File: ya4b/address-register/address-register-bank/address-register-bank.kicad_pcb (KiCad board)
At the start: 4 copper layers, 114.3 x 90.3 mm, 99 parts, among them J1 Conn_01x38_Male, U1 GAL16V8, U10 74LS169, U11 74LS169, U12 74LS541, U13 74LS169, U14 74LS169, U15 74LS541, U16 74LS169, U17 74LS169, U18 74LS541, U2 GAL22V10, U3 74HCT04, U4 74HCT00, U5 74LS157, U6 74LS157, U7 74LS169, U8 74LS169, U9 74LS541

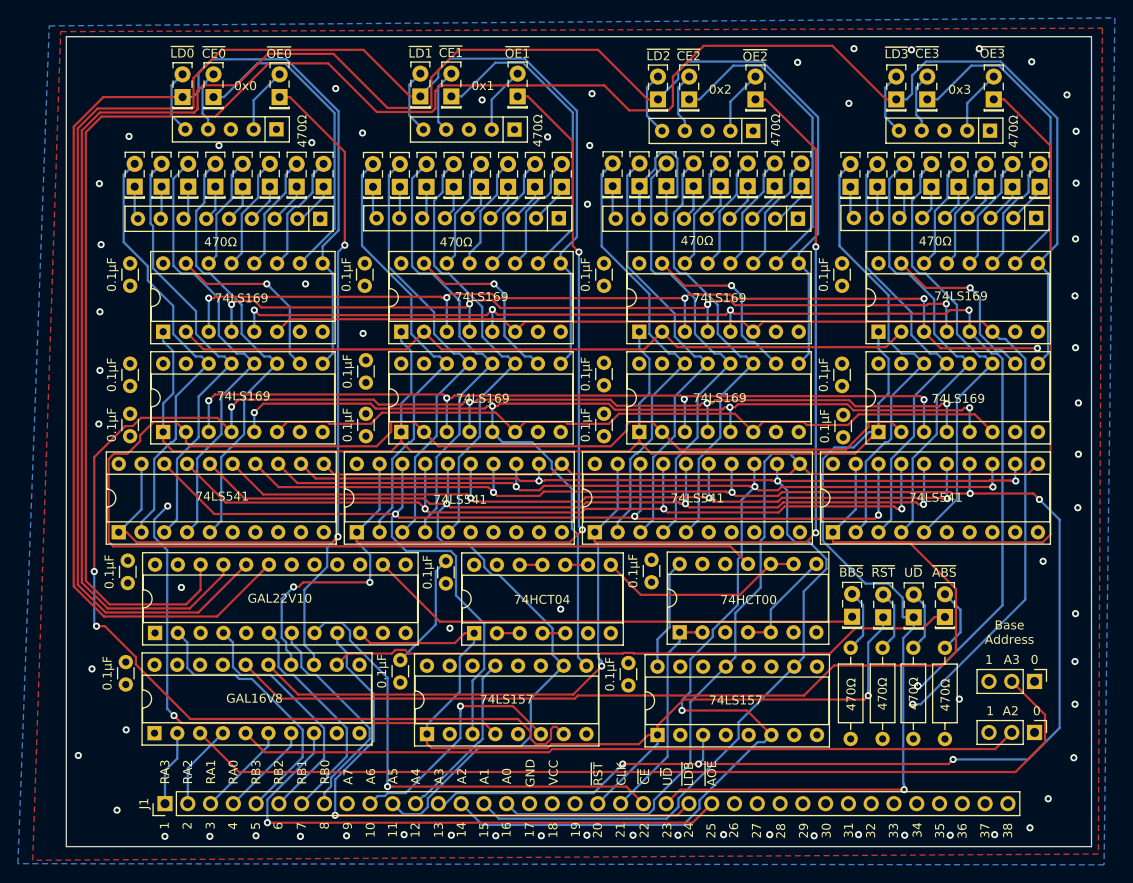
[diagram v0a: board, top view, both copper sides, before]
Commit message: Fixed PCB design files for address register bank
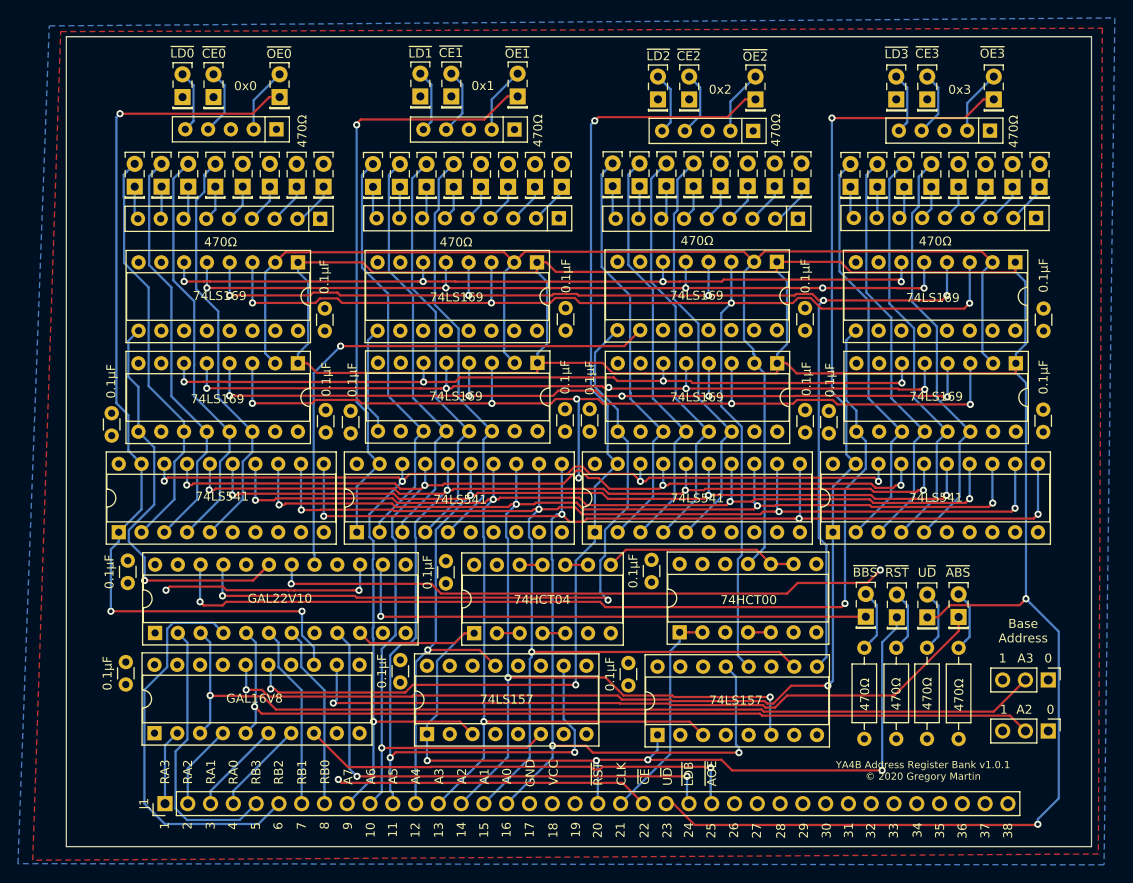
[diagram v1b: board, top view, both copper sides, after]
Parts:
- moved C13 102.1 mm to (-49.8, 50.6), turned to 90 degrees
- moved C7 102.1 mm to (-49.8, 61.8), turned to 90 degrees
- moved C14 19.3 mm to (-129.8, 61.9), turned to 90 degrees
- moved U14 17.2 mm to (-79.5, 42.9), turned to 270 degrees
- moved U13 17.2 mm to (-79.5, 54.2), turned to 270 degrees
- moved U16 17.1 mm to (-52.9, 54.2), turned to 270 degrees
- moved U17 17.1 mm to (-52.9, 42.9), turned to 270 degrees
- moved U10 17.0 mm to (-106.2, 54.1), turned to 270 degrees
- moved U11 17.0 mm to (-106.3, 42.9), turned to 270 degrees
- moved U8 16.9 mm to (-132.9, 42.9), turned to 270 degrees
- moved U7 16.9 mm to (-132.9, 54.2), turned to 270 degrees
- moved C12 8.80 mm to (-103.1, 61.8), turned to 90 degrees
- moved C17 8.70 mm to (-76.4, 61.9), turned to 90 degrees
- moved C15 8.62 mm to (-103.1, 50.5), turned to 90 degrees
- moved C18 8.54 mm to (-76.4, 50.5), turned to 90 degrees
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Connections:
- D10 pad 2: Net-(D10-Pad2) -> /R0_2
- D11 pad 2: Net-(D11-Pad2) -> /R0_1
- D12 pad 2: Net-(D12-Pad2) -> /R0_0
- D17 pad 2: Net-(D17-Pad2) -> /R1_7
- D18 pad 2: Net-(D18-Pad2) -> /R1_6
- D19 pad 2: Net-(D19-Pad2) -> /R1_5
- D20 pad 2: Net-(D20-Pad2) -> /R1_4
- D21 pad 2: Net-(D21-Pad2) -> /R1_3
- D22 pad 2: Net-(D22-Pad2) -> /R1_2
- D23 pad 2: Net-(D23-Pad2) -> /R1_1
- D24 pad 2: Net-(D24-Pad2) -> /R1_0
- D29 pad 2: Net-(D29-Pad2) -> /R2_7
- D30 pad 2: Net-(D30-Pad2) -> /R2_6
- D31 pad 2: Net-(D31-Pad2) -> /R2_5
- D32 pad 2: Net-(D32-Pad2) -> /R2_4
- D33 pad 2: Net-(D33-Pad2) -> /R2_3
- D34 pad 2: Net-(D34-Pad2) -> /R2_2
- D35 pad 2: Net-(D35-Pad2) -> /R2_1
- D36 pad 2: Net-(D36-Pad2) -> /R2_0
- D41 pad 2: Net-(D41-Pad2) -> /R3_7
- D42 pad 2: Net-(D42-Pad2) -> /R3_6
- D43 pad 2: Net-(D43-Pad2) -> /R3_5
- D44 pad 2: Net-(D44-Pad2) -> /R3_4
- D45 pad 2: Net-(D45-Pad2) -> /R3_3
- D46 pad 2: Net-(D46-Pad2) -> /R3_2
- D47 pad 2: Net-(D47-Pad2) -> /R3_1
- D48 pad 2: Net-(D48-Pad2) -> /R3_0
- D5 pad 2: Net-(D5-Pad2) -> /R0_7
- D6 pad 2: Net-(D6-Pad2) -> /R0_6
- D7 pad 2: Net-(D7-Pad2) -> /R0_5
- D8 pad 2: Net-(D8-Pad2) -> /R0_4
- D9 pad 2: Net-(D9-Pad2) -> /R0_3
- U10 pad 11: Net-(D20-Pad2) -> /R1_7
- U10 pad 12: Net-(D19-Pad2) -> /R1_6
- U10 pad 13: Net-(D18-Pad2) -> /R1_5
- U10 pad 14: Net-(D17-Pad2) -> /R1_4
- U10 pad 3: AI7 -> AI4
- U10 pad 4: AI6 -> AI5
- U10 pad 5: AI5 -> AI6
- U10 pad 6: AI4 -> AI7
- U11 pad 11: Net-(D24-Pad2) -> /R1_3
- U11 pad 12: Net-(D23-Pad2) -> /R1_2
- U11 pad 13: Net-(D22-Pad2) -> /R1_1
- U11 pad 14: Net-(D21-Pad2) -> /R1_0
- U11 pad 3: AI3 -> AI0
- U11 pad 4: AI2 -> AI1
- U11 pad 5: AI1 -> AI2
- U11 pad 6: AI0 -> AI3
- U12 pad 2: Net-(D17-Pad2) -> /R1_7
- U12 pad 3: Net-(D18-Pad2) -> /R1_6
- U12 pad 4: Net-(D19-Pad2) -> /R1_5
- U12 pad 5: Net-(D20-Pad2) -> /R1_4
- U12 pad 6: Net-(D21-Pad2) -> /R1_3
- U12 pad 7: Net-(D22-Pad2) -> /R1_2
- U12 pad 8: Net-(D23-Pad2) -> /R1_1
- U12 pad 9: Net-(D24-Pad2) -> /R1_0
- U13 pad 11: Net-(D32-Pad2) -> /R2_7
- U13 pad 12: Net-(D31-Pad2) -> /R2_6
- U13 pad 13: Net-(D30-Pad2) -> /R2_5
- U13 pad 14: Net-(D29-Pad2) -> /R2_4
- U13 pad 3: AI7 -> AI4
- U13 pad 4: AI6 -> AI5
- U13 pad 5: AI5 -> AI6
- U13 pad 6: AI4 -> AI7
- U14 pad 11: Net-(D36-Pad2) -> /R2_3
- U14 pad 12: Net-(D35-Pad2) -> /R2_2
- U14 pad 13: Net-(D34-Pad2) -> /R2_1
- U14 pad 14: Net-(D33-Pad2) -> /R2_0
- U14 pad 3: AI3 -> AI0
- U14 pad 4: AI2 -> AI1
- U14 pad 5: AI1 -> AI2
- U14 pad 6: AI0 -> AI3
- U15 pad 2: Net-(D29-Pad2) -> /R2_7
- U15 pad 3: Net-(D30-Pad2) -> /R2_6
- U15 pad 4: Net-(D31-Pad2) -> /R2_5
- U15 pad 5: Net-(D32-Pad2) -> /R2_4
- U15 pad 6: Net-(D33-Pad2) -> /R2_3
- U15 pad 7: Net-(D34-Pad2) -> /R2_2
- U15 pad 8: Net-(D35-Pad2) -> /R2_1
- U15 pad 9: Net-(D36-Pad2) -> /R2_0
- U16 pad 11: Net-(D44-Pad2) -> /R3_7
- U16 pad 12: Net-(D43-Pad2) -> /R3_6
- U16 pad 13: Net-(D42-Pad2) -> /R3_5
- U16 pad 14: Net-(D41-Pad2) -> /R3_4
- U16 pad 3: AI7 -> AI4
- U16 pad 4: AI6 -> AI5
- U16 pad 5: AI5 -> AI6
- U16 pad 6: AI4 -> AI7
- U17 pad 11: Net-(D48-Pad2) -> /R3_3
- U17 pad 12: Net-(D47-Pad2) -> /R3_2
- U17 pad 13: Net-(D46-Pad2) -> /R3_1
- U17 pad 14: Net-(D45-Pad2) -> /R3_0
- U17 pad 3: AI3 -> AI0
- U17 pad 4: AI2 -> AI1
- U17 pad 5: AI1 -> AI2
- U17 pad 6: AI0 -> AI3
- U18 pad 2: Net-(D41-Pad2) -> /R3_7
- U18 pad 3: Net-(D42-Pad2) -> /R3_6
- U18 pad 4: Net-(D43-Pad2) -> /R3_5
- U18 pad 5: Net-(D44-Pad2) -> /R3_4
- U18 pad 6: Net-(D45-Pad2) -> /R3_3
- U18 pad 7: Net-(D46-Pad2) -> /R3_2
- U18 pad 8: Net-(D47-Pad2) -> /R3_1
- U18 pad 9: Net-(D48-Pad2) -> /R3_0
- U7 pad 11: Net-(D8-Pad2) -> /R0_7
- U7 pad 12: Net-(D7-Pad2) -> /R0_6
- U7 pad 13: Net-(D6-Pad2) -> /R0_5
- U7 pad 14: Net-(D5-Pad2) -> /R0_4
- U7 pad 3: AI7 -> AI4
- U7 pad 4: AI6 -> AI5
- U7 pad 5: AI5 -> AI6
- U7 pad 6: AI4 -> AI7
- U8 pad 11: Net-(D12-Pad2) -> /R0_3
- U8 pad 12: Net-(D11-Pad2) -> /R0_2
- U8 pad 13: Net-(D10-Pad2) -> /R0_1
- U8 pad 14: Net-(D9-Pad2) -> /R0_0
- U8 pad 3: AI3 -> AI0
- U8 pad 4: AI2 -> AI1
- U8 pad 5: AI1 -> AI2
- U8 pad 6: AI0 -> AI3
- U9 pad 2: Net-(D5-Pad2) -> /R0_7
- U9 pad 3: Net-(D6-Pad2) -> /R0_6
- U9 pad 4: Net-(D7-Pad2) -> /R0_5
- U9 pad 5: Net-(D8-Pad2) -> /R0_4
- U9 pad 6: Net-(D9-Pad2) -> /R0_3
- U9 pad 7: Net-(D10-Pad2) -> /R0_2
- U9 pad 8: Net-(D11-Pad2) -> /R0_1
- U9 pad 9: Net-(D12-Pad2) -> /R0_0
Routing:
- net GND: track 558.2 -> 0.00 mm, vias 64 -> 0
- net VCC: track 468.6 -> 137.9 mm
- net REGCLK: track 278.0 -> 155.3 mm
- net U~D~: track 213.1 -> 326.7 mm, vias 1 -> 2
- net ~LD1~: track 171.0 -> 65.7 mm
- net ~LD2~: track 200.4 -> 109.2 mm, vias 0 -> 2
- net ~LD3~: track 226.8 -> 138.2 mm, vias 0 -> 2
- net ~LD0~: track 142.8 -> 74.8 mm, vias 0 -> 1
- net AI6: track 190.9 -> 132.4 mm, vias 6 -> 5
- net Net-(D31-Pad2): track 49.9 -> 0.00 mm
- net Net-(D7-Pad2): track 49.9 -> 0.00 mm
- net Net-(D19-Pad2): track 49.8 -> 0.00 mm
- net Net-(D43-Pad2): track 49.8 -> 0.00 mm
- net Net-(D20-Pad2): track 49.6 -> 0.00 mm
- net Net-(D41-Pad2): track 49.6 -> 0.00 mm
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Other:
- board text added: "YA4B Address Register Bank v1.0.1 © 2020 Gregory Martin"
